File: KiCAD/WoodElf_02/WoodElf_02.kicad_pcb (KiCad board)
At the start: 2 copper layers, 19.2 x 19.2 mm, 21 parts

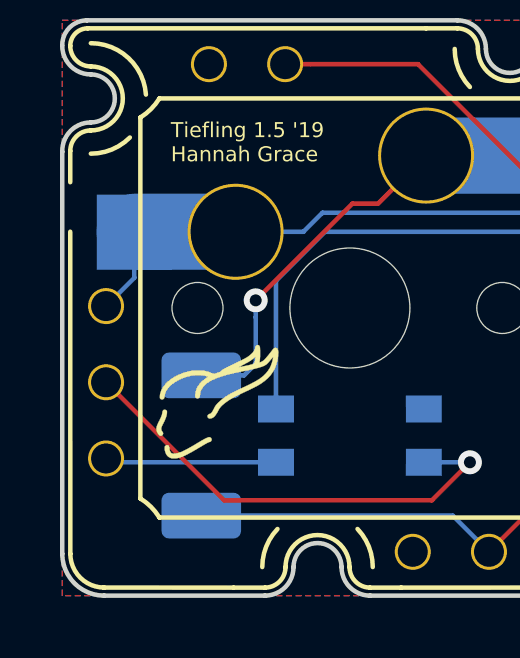
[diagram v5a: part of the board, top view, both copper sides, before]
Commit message: fixed location of joystick pcb in folder
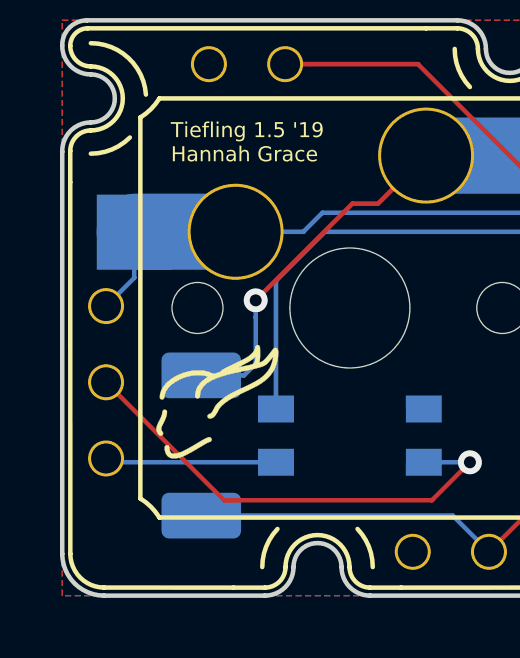
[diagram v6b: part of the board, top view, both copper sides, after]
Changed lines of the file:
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@@
       (xy 0.818239 1.280587) (xy 0.836527 1.277357)) (layer B.SilkS) (width 0.01))
   )
+  (gr_arc (start 60.2615 30.6959) (end 59.309 30.6959) (angle -90) (layer Edge.Cuts) (width 0.15))
   (gr_line (start 60.071 30.607) (end 60.071 48.26) (layer B.CrtYd) (width 0.15))
   (gr_line (start 77.724 30.607) (end 60.071 30.607) (layer B.CrtYd) (width 0.15))
@@
   (gr_line (start 60.1599 30.1117) (end 71.44004 30.1117) (layer B.SilkS) (width 0.15))
   (gr_arc (start 60.1599 30.6959) (end 60.1599 30.1117) (angle -90) (layer B.SilkS) (width 0.15))
-  (gr_line (start 59.57316 47.61992) (end 59.57062 36.88588) (layer B.SilkS) (width 0.15))
+  (gr_line (start 59.57316 47.61992) (end 59.5757 35.2425) (layer B.SilkS) (width 0.15))
   (gr_arc (start 60.70346 47.625) (end 59.5757 47.625) (angle -90) (layer B.SilkS) (width 0.15))
   (gr_line (start 77.089 48.75022) (end 70.612 48.7553) (layer B.SilkS) (width 0.15))
@@
   (gr_line (start 77.089 48.75276) (end 70.5993 48.7553) (layer F.SilkS) (width 0.15))
   (gr_arc (start 60.706 47.625) (end 59.57824 47.625) (angle -90) (layer F.SilkS) (width 0.15))
-  (gr_line (start 59.57824 47.625) (end 59.5757 36.89096) (layer F.SilkS) (width 0.15))
+  (gr_line (start 59.57824 47.625) (end 59.5757 35.2425) (layer F.SilkS) (width 0.15))
   (gr_line (start 60.70092 48.75276) (end 65.024 48.7553) (layer B.SilkS) (width 0.15))
   (gr_line (start 60.1599 30.1117) (end 71.44004 30.1117) (layer F.SilkS) (width 0.15))
@@
   (gr_line (start 78.21676 31.242) (end 78.2193 41.97604) (layer F.SilkS) (width 0.15))
   (gr_arc (start 77.089 31.242) (end 78.21676 31.242) (angle -90) (layer F.SilkS) (width 0.15))
-  (gr_arc (start 60.2615 30.6959) (end 59.309 30.6959) (angle -90) (layer Edge.Cuts) (width 0.15))
   (gr_arc (start 60.2615 32.4485) (end 60.2615 33.2486) (angle -180) (layer Edge.Cuts) (width 0.15))
   (gr_arc (start 60.2615 34.2011) (end 60.2615 33.2486) (angle -91.52752544) (layer Edge.Cuts) (width 0.15))

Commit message: working out how to mount the joystick to the sandwich
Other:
- outline, holes or cut-outs redrawn

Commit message: workin'
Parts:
- DIN1, DO1, GND1 (x2), SWIN1 (x2), SWO1 (x2), VDD1 (x2): value BlankThrough-Hole -> BTH
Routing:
- net Net-(D1-Pad1): track 14.9 -> 24.5 mm
- net /DIN: track 15.9 -> 17.3 mm
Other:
- outline, holes or cut-outs redrawn
- board text added: "Tiefling 1.6 Cora Grace"
- board text removed: "Tiefling 1.5 '19 Hannah Grace"
